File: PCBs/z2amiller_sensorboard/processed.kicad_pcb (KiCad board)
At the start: 2 copper layers, 48.9 x 19.3 mm, 25 parts, among them P1 PWR, P2 PROG, U1 ESP-07v2, U2 LMR16006Y, U3 BME280

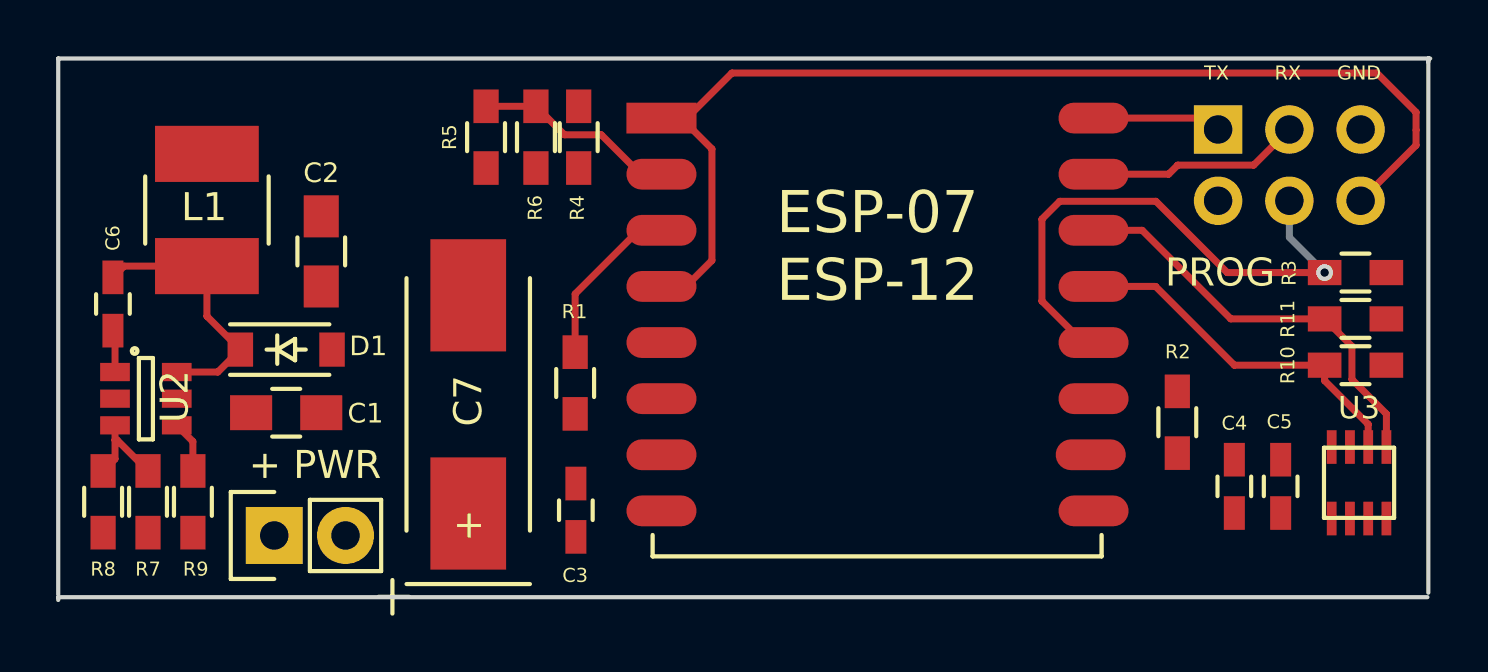
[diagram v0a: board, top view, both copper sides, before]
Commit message: recheck all circuits and clean up fill zone by rerouting the nets using freerouting and manually
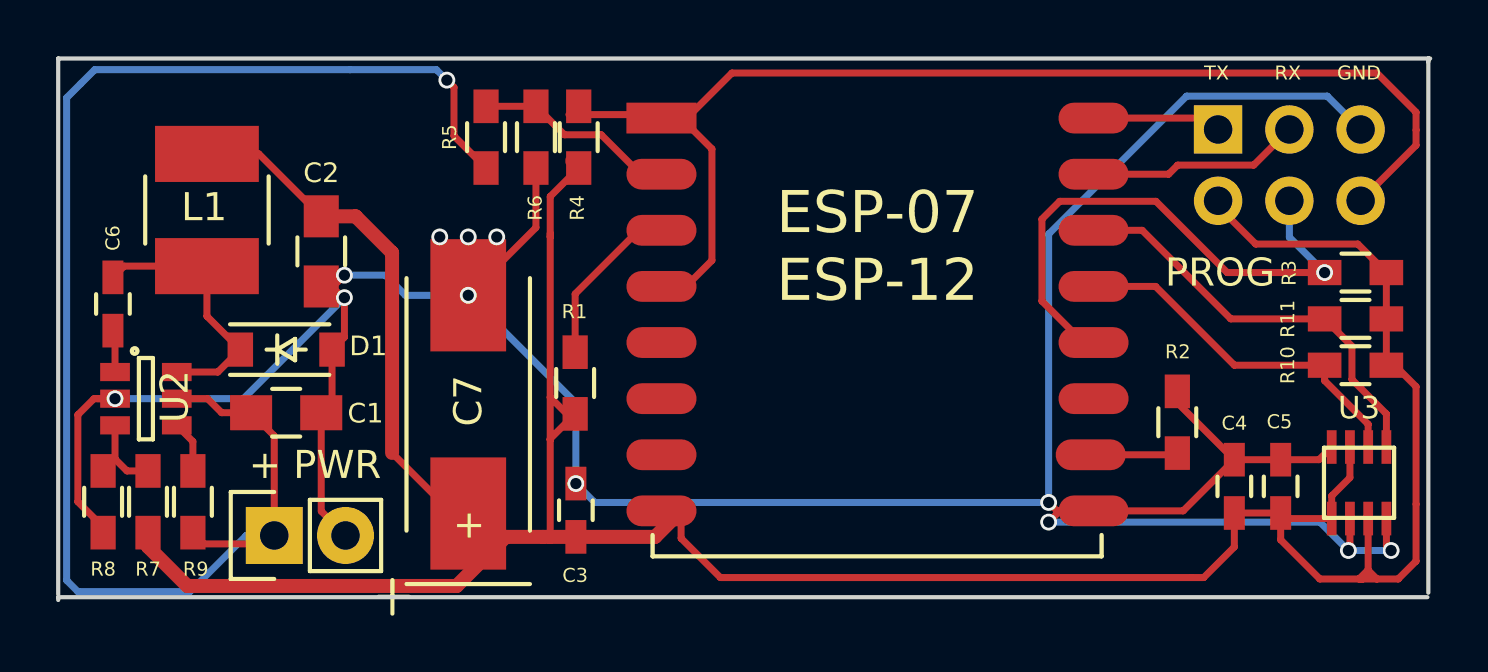
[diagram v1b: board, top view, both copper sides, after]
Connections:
- C1 pad 1: (no net) -> +6V
- C1 pad 2: (no net) -> GND
- C2 pad 1: (no net) -> +3V3
- C2 pad 2: (no net) -> GND
- C3 pad 1: (no net) -> +3V3
- C3 pad 2: (no net) -> GND
- C4 pad 1: (no net) -> GND
- C4 pad 2: (no net) -> +3V3
- C5 pad 1: (no net) -> GND
- C5 pad 2: (no net) -> +3V3
- C7 pad 1: (no net) -> +3V3
- C7 pad 2: (no net) -> GND
- D1 pad 2: (no net) -> GND
- L1 pad 2: (no net) -> +3V3
- P1 pad 1: (no net) -> +6V
- P1 pad 2: (no net) -> GND
- P2 pad 2: (no net) -> +3V3
- P2 pad 5: (no net) -> GND
- R1 pad 1: (no net) -> +3V3
- R10 pad 2: (no net) -> +3V3
- R11 pad 2: (no net) -> +3V3
- R2 pad 1: (no net) -> GPIO15
- R2 pad 2: (no net) -> GND
- R3 pad 1: (no net) -> +3V3
- R4 pad 1: (no net) -> +3V3
- R4 pad 2: (no net) -> GPIO16
- R5 pad 1: (no net) -> +6V
- R6 pad 2: (no net) -> GND
- R7 pad 1: (no net) -> +3V3
- R8 pad 2: (no net) -> GND
- R9 pad 1: (no net) -> +6V
- U1 pad 10: (no net) -> GPIO15
- U1 pad 11: (no net) -> Net-(U1-Pad11)
- U1 pad 5: (no net) -> Net-(U1-Pad5)
- U1 pad 6: (no net) -> Net-(U1-Pad6)
- U1 pad 7: (no net) -> Net-(U1-Pad7)
- U1 pad 8: (no net) -> +3V3
- U1 pad 9: (no net) -> GND
- U2 pad 2: (no net) -> GND
- U2 pad 5: (no net) -> +6V
- U3 pad 1: (no net) -> GND
- U3 pad 2: (no net) -> +3V3
- U3 pad 5: (no net) -> GND
- U3 pad 6: (no net) -> +3V3
- U3 pad 7: (no net) -> GND
- U3 pad 8: (no net) -> +3V3
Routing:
- net GND: track 0.00 -> 123.6 mm, vias 0 -> 12
- net +3V3: track 0.00 -> 113.2 mm
- net +6V: track 0.00 -> 54.1 mm, vias 0 -> 1
- net GPIO16: track 38.4 -> 42.5 mm
- net GPIO15: track 0.00 -> 3.57 mm
- net ADC_IN: track 7.95 -> 9.63 mm
- net CH_PD: track 6.79 -> 8.27 mm
- net SDL: track 15.7 -> 17.1 mm
- net SDA: track 13.7 -> 14.8 mm
- net GPIO0: track 19.3 -> 19.9 mm
